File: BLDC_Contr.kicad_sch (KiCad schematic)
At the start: 100 parts, among them J1 XT60, J10 PH, J2 MR60, J3 Conn_ARM_SWD_TagConnect_TC2030, J4 PH, J5 PH, J6 PH, J7 PH, J8 PH, J9 PIN, Q1 CSD18540Q5B, Q2 CSD18540Q5B, Q3 CSD18540Q5B, Q4 CSD18540Q5B, Q5 CSD18540Q5B, Q6 CSD18540Q5B, U1 STM32G431CBU6, U2 DRV8323RSRGZR, U3 AMS1117-3.3, Y1 Crystal_16Mhz

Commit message: add PCB layouts
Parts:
- removed C2: 0.1u, Capacitor_SMD:C_0603_1608Metric, symbol Device:C_Small
- removed J2: MR60, Connector_AMASS:AMASS_MR30PW-M_1x03_P3.50mm_Horizontal, symbol Connector_Generic:Conn_01x03
- added H5, H6, H7: MountingHole_Pad_MP, MountingHole:MountingHole_2.5mm_Pad_Via, symbol Mechanical:MountingHole_Pad_MP
- C18: renamed from C19; footprint Capacitor_SMD:C_0603_1608Metric -> Capacitor_SMD:C_1210_3225Metric
- C19: renamed from C20; footprint Capacitor_SMD:C_0603_1608Metric -> Capacitor_SMD:C_1210_3225Metric
- D10, D13, D6, D8: footprint Package_TO_SOT_SMD:SOT-143 -> Diode_SMD:Nexperia_DSN1608-2_1.6x0.8mm; symbol Device:D_TVS -> Diode:PTVS5V0Z1USK
- D11: footprint Diode_SMD:D_0201_0603Metric -> Package_TO_SOT_SMD:SOT-23
- D12, D4, D5, D7, D9: footprint Package_TO_SOT_SMD:SOT-23-3 -> Package_TO_SOT_SMD:SOT-523
- J10: footprint Connector_JST:JST_PH_S4B-PH-K_1x04_P2.00mm_Horizontal -> Connector_JST:JST_PH_S5B-PH-K_1x05_P2.00mm_Horizontal
- J2: renamed from J3; footprint Connector:Tag-Connect_TC2030-IDC-FP_2x03_P1.27mm_Vertical -> Connector:Tag-Connect_TC2030-IDC-NL_2x03_P1.27mm_Vertical
- R10, R11, R12: value 3m -> 1m
- R21, R22: value 0 -> 56
- renumbered C11 to C10, C12 to C11, C13 to C12, C14 to C13, C15 to C14, C16 to C15, C17 to C16, C18 to C17, C3 to C2, C21 to C20, C22 to C21, C23 to C22, C24 to C23, C25 to C24, C26 to C25, C27 to C26, C28 to C27, C29 to C28, C30 to C29, C4 to C3, C36 to C30, C5 to C4, C6 to C5, C7 to C6, C8 to C7, C9 to C8, C10 to C9, J4 to J3, J5 to J4, J6 to J5, J7 to J6, J8 to J7, J9 to J8, Q2 to Q1, Q1 to Q2, Q4 to Q3, Q3 to Q4, Q6 to Q5, Q5 to Q6, R16 to R13, R13 to R14, R14 to R15, R15 to R16
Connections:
- net +3.3V: now also D10.1 (K), D6.1 (K), D8.1 (K); no longer C17.1, D10.2 (A2), D6.2 (A2), D8.2 (A2), U2.26 (VREF)
- net +3.3VA: now also C17.1, U2.26 (VREF)
- net +5V: now also D13.1 (K); no longer D13.2 (A2)
- net AMT_A_C: now also D12.1 (K); no longer D12.2 (K)
- net AMT_B_C: now also D12.2 (K); no longer D12.1 (K)
- net CAN_H_C: now also D11.2 (A2), J6.2 (Pin_2), J7.2 (Pin_2); no longer D11.1 (A1), J6.1 (Pin_1), J7.1 (Pin_1)
- net CAN_L_C: now also D11.1 (A1), J6.1 (Pin_1), J7.1 (Pin_1); no longer D11.2 (A2), J6.2 (Pin_2), J7.2 (Pin_2)
- net GND: now also D10.2 (A), D13.2 (A), D6.2 (A), D8.2 (A); no longer D10.1 (A1), D13.1 (A1), D6.1 (A1), D8.1 (A1)
- net SHA: now also H5.MP
- net SHB: now also H7.MP
- net SHC: now also H6.MP
- net SPI1_MISO_C: now also D5.2 (K); no longer D5.1 (K)
- net SPI1_MOSI_C: now also D4.1 (K); no longer D4.2 (K)
- net SPI1_NCS_C: now also D4.2 (K); no longer D4.1 (K)
- net SPI1_SCK_C: now also D5.1 (K); no longer D5.2 (K)
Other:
- moved on the sheet: C1, D10, D13, D6, D8

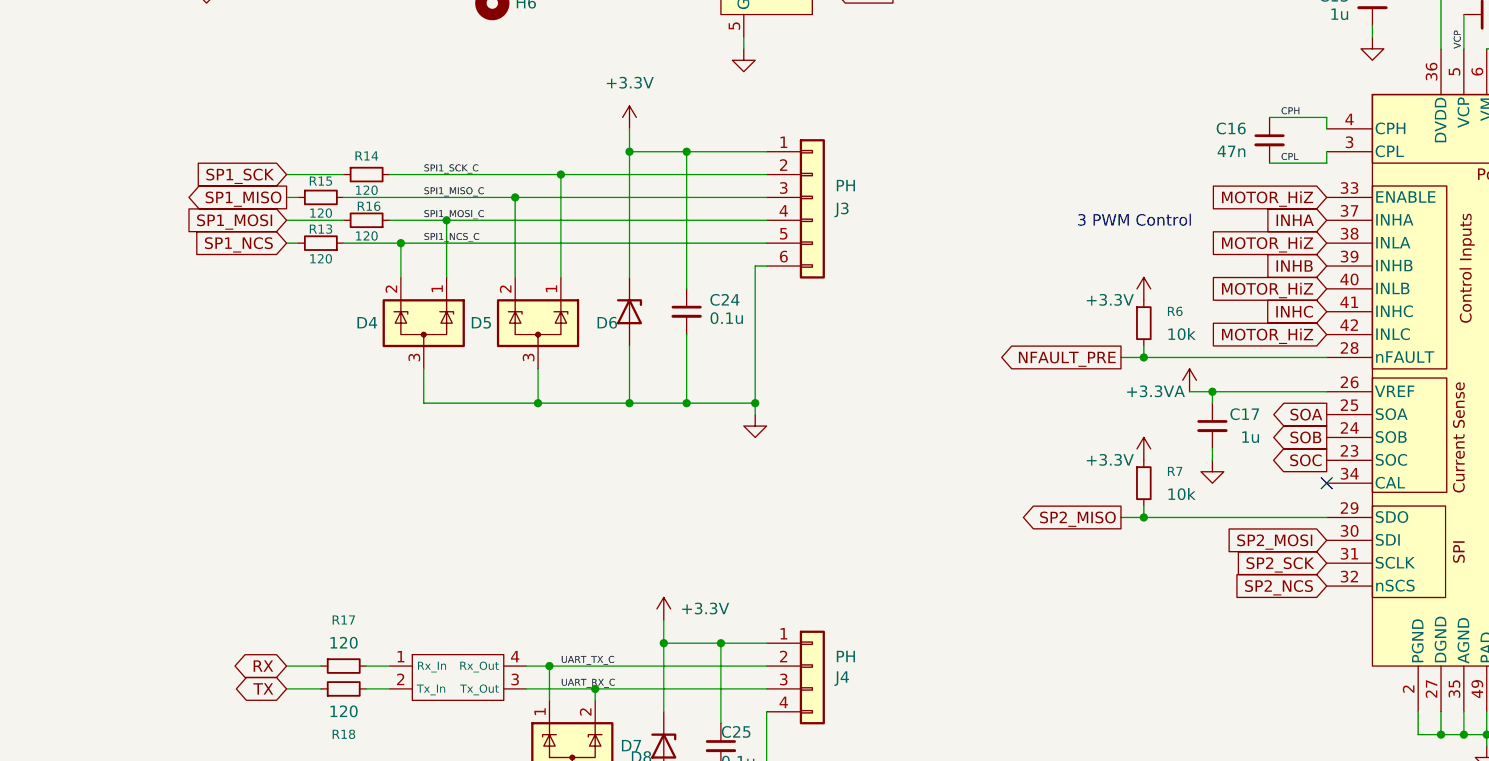
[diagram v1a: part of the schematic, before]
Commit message: add wiring. changed communication of spi on drv8323 from spi2 to spi1 for better wiring.
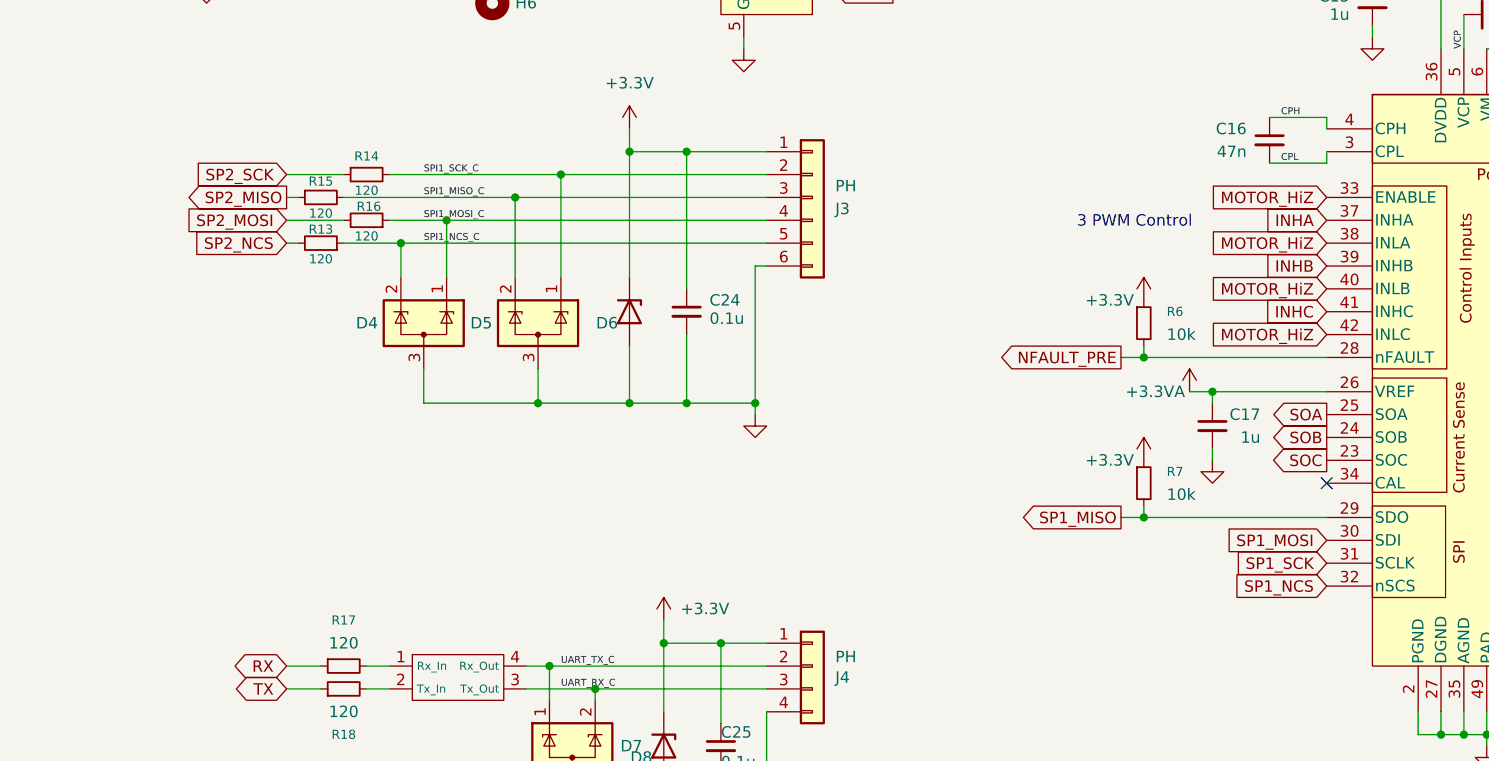
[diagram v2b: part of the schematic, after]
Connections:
- net SP1_MISO: now also R7.2, U2.29 (SDO); no longer R15.1
- net SP1_MOSI: now also U2.30 (SDI); no longer R16.2
- net SP1_NCS: now also U2.32 (nSCS); no longer R13.2
- net SP1_SCK: now also U2.31 (SCLK); no longer R14.1
- net SP2_MISO: now also R15.1; no longer R7.2, U2.29 (SDO)
- net SP2_MOSI: now also R16.2; no longer U2.30 (SDI)
- net SP2_NCS: now also R13.2; no longer U2.32 (nSCS)
- net SP2_SCK: now also R14.1; no longer U2.31 (SCLK)

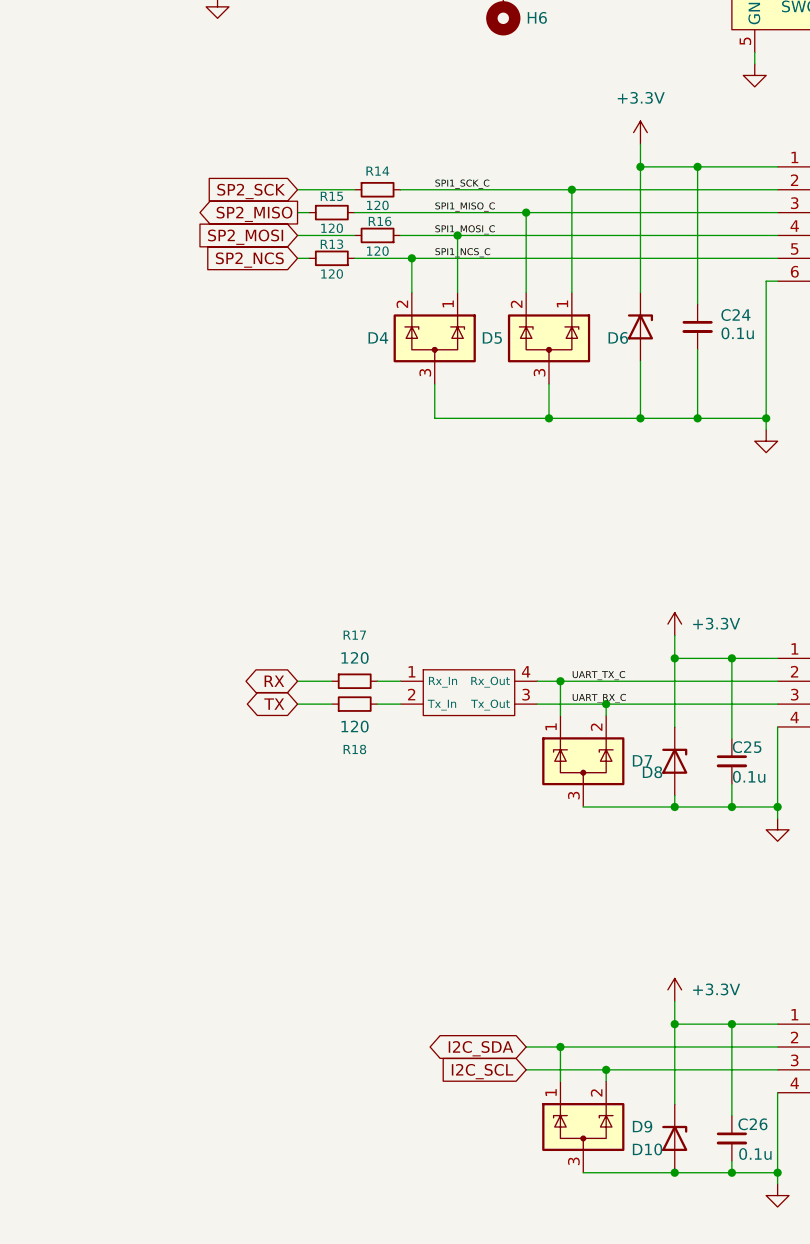
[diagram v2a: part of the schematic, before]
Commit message: added most wiring, not erc checked. changed pinouts on connectors for easier wiring
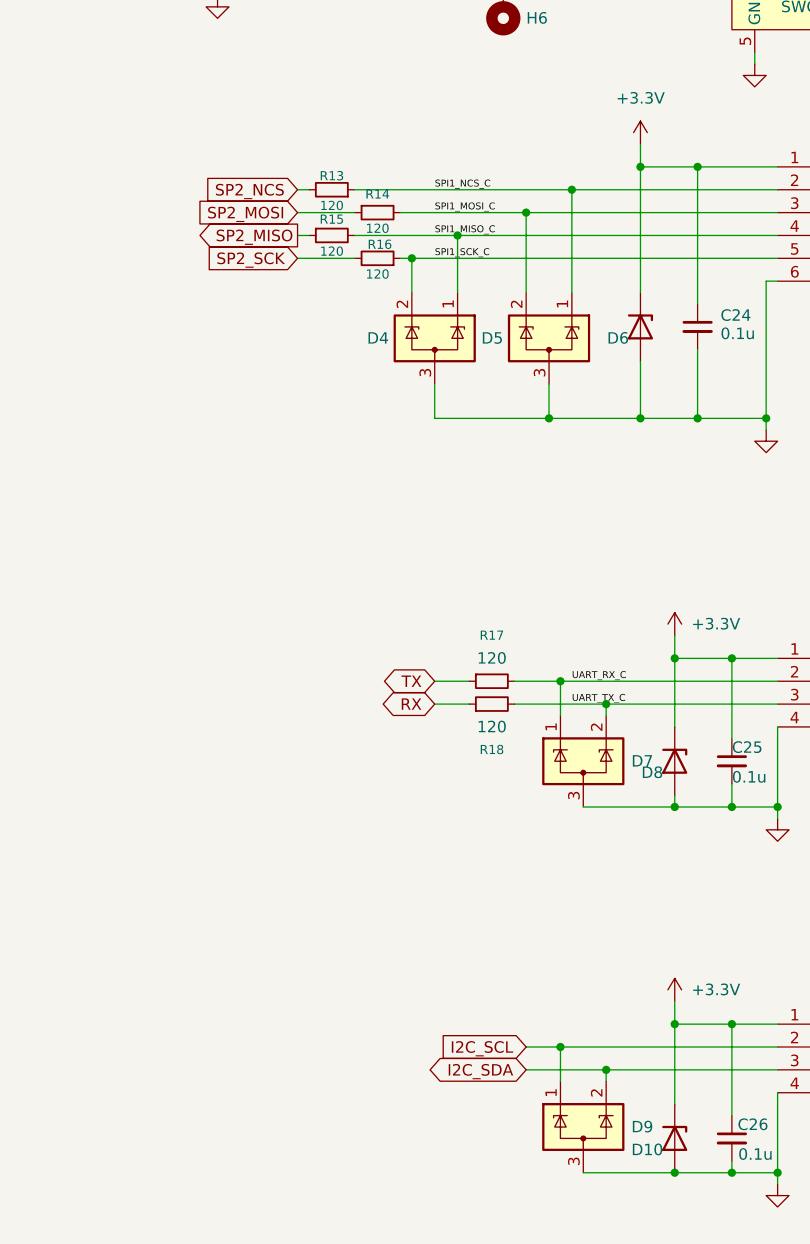
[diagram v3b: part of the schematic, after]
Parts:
- removed U5: ~, poka-yoke_rxtx:poka-yoke_rxtx, symbol poka-yoke_rxtx:poka_yoke_txrx
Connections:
- net I2C_SCL: now also D9.1 (K), J5.2 (Pin_2); no longer D9.2 (K), J5.3 (Pin_3)
- net I2C_SDA: now also D9.2 (K), J5.3 (Pin_3); no longer D9.1 (K), J5.2 (Pin_2)
- net RX: now also R18.1; no longer R17.1
- net SP2_MOSI: now also R14.1; no longer R16.2
- net SP2_SCK: now also R16.2; no longer R14.1
- net SPI1_MISO_C: now also D4.1 (K), J3.4 (Pin_4); no longer D5.2 (K), J3.3 (Pin_3)
- net SPI1_MOSI_C: now also D5.2 (K), J3.3 (Pin_3), R14.2; no longer D4.1 (K), J3.4 (Pin_4), R16.1
- net SPI1_NCS_C: now also D5.1 (K), J3.2 (Pin_2); no longer D4.2 (K), J3.5 (Pin_5)
- net SPI1_SCK_C: now also D4.2 (K), J3.5 (Pin_5), R16.1; no longer D5.1 (K), J3.2 (Pin_2), R14.2
- net TX: now also R17.1; no longer R18.1
- net UART_RX_C: now also D7.1 (K), J4.2 (Pin_2), R17.2; no longer D7.2 (K), J4.3 (Pin_3)
- net UART_TX_C: now also D7.2 (K), J4.3 (Pin_3), R18.2; no longer D7.1 (K), J4.2 (Pin_2)
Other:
- moved on the sheet: R13, R14, R15, R16, R17, R18

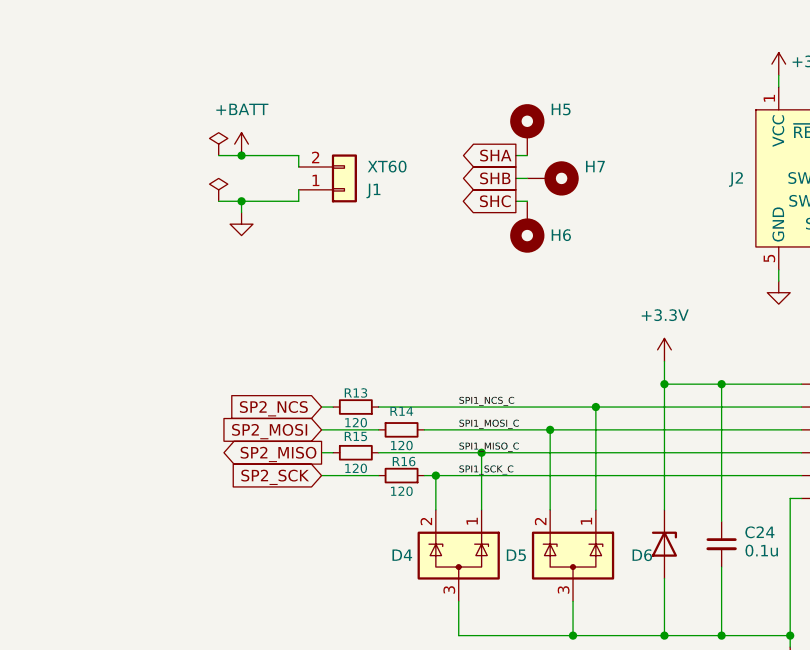
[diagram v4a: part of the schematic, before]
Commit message: changed most 0603 parts to 0402. wiring changed. pcb dimesion from 65*80mm to 60*80mm
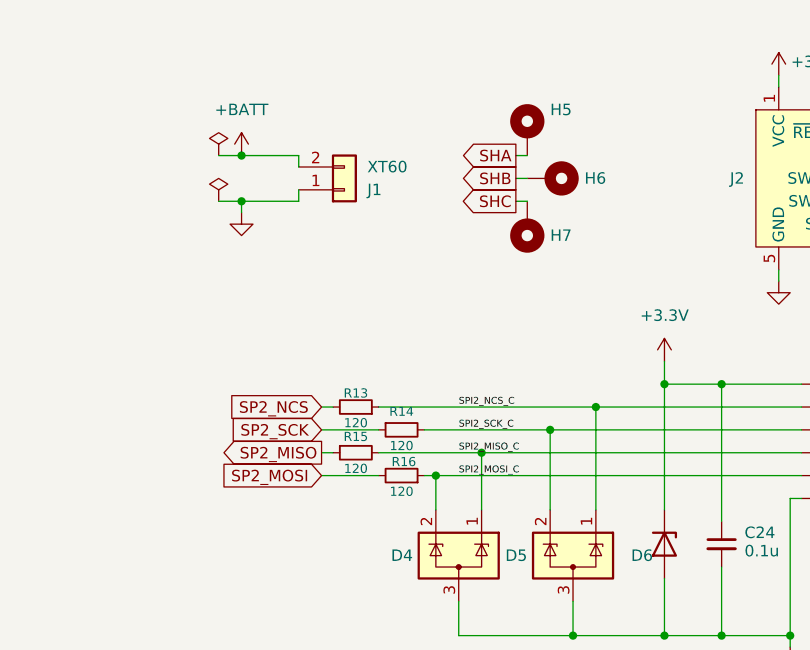
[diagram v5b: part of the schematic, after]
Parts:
- C1, C10, C11, C12, C13, C14, C15, C17, C2, C20, C23, C24, C25, C26, C27, C28, C29, C3, C4, C5, C7, C8, C9: footprint Capacitor_SMD:C_0603_1608Metric -> Capacitor_SMD:C_0402_1005Metric
- H1, H2, H3, H4: footprint MountingHole:MountingHole_3.2mm_M3_DIN965_Pad_TopBottom -> MountingHole:MountingHole_3.2mm_M3_Pad_Via
- R1, R13, R14, R15, R16, R17, R18, R19, R2, R20, R21, R22, R3, R4, R5, R6, R7, R8: footprint Resistor_SMD:R_0603_1608Metric -> Resistor_SMD:R_0402_1005Metric
- R9: footprint Resistor_SMD:R_0603_1608Metric -> Resistor_SMD:R_0805_2012Metric
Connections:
- net SHB: now also H6.MP; no longer H7.MP
- net SHC: now also H7.MP; no longer H6.MP
- net SP2_MOSI: now also R16.2; no longer R14.1
- net SP2_SCK: now also R14.1; no longer R16.2
- net SPI1_MISO_C renamed SPI2_MISO_C
- net SPI1_MOSI_C renamed SPI2_SCK_C
- net SPI1_NCS_C renamed SPI2_NCS_C
- net SPI1_SCK_C renamed SPI2_MOSI_C
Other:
- moved on the sheet: H6, H7

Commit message: DRCing not done
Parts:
- H1, H2, H3, H4: footprint MountingHole:MountingHole_3.2mm_M3_Pad_Via -> MountingHole:MountingHole_3.2mm_M3_Pad_TopBottom
- H5, H6, H7: footprint MountingHole:MountingHole_2.5mm_Pad_Via -> MountingHole:MountingHole_2.5mm_Pad_TopBottom
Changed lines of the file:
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@@
 			)
 		)
-		(property "Footprint" "MountingHole:MountingHole_2.5mm_Pad_Via"
+		(property "Footprint" "MountingHole:MountingHole_2.5mm_Pad_TopBottom"
 			(at 194.31 39.37 0)
 			(effects
@@
 			)
 		)
-		(property "Footprint" "MountingHole:MountingHole_3.2mm_M3_Pad_Via"
+		(property "Footprint" "MountingHole:MountingHole_3.2mm_M3_Pad_TopBottom"
 			(at 76.2 232.41 0)
 			(effects
@@
 			)
 		)
-		(property "Footprint" "MountingHole:MountingHole_2.5mm_Pad_Via"
+		(property "Footprint" "MountingHole:MountingHole_2.5mm_Pad_TopBottom"
 			(at 196.85 34.29 0)
 			(effects
@@
 			)
 		)
-		(property "Footprint" "MountingHole:MountingHole_2.5mm_Pad_Via"
+		(property "Footprint" "MountingHole:MountingHole_2.5mm_Pad_TopBottom"
 			(at 194.31 29.21 0)
 			(effects
@@
 			)
 		)
-		(property "Footprint" "MountingHole:MountingHole_3.2mm_M3_Pad_Via"
+		(property "Footprint" "MountingHole:MountingHole_3.2mm_M3_Pad_TopBottom"
 			(at 63.5 232.41 0)
 			(effects
@@
 			)
 		)
-		(property "Footprint" "MountingHole:MountingHole_3.2mm_M3_Pad_Via"
+		(property "Footprint" "MountingHole:MountingHole_3.2mm_M3_Pad_TopBottom"
 			(at 101.6 232.41 0)
 			(effects
@@
 			)
 		)
-		(property "Footprint" "MountingHole:MountingHole_3.2mm_M3_Pad_Via"
+		(property "Footprint" "MountingHole:MountingHole_3.2mm_M3_Pad_TopBottom"
 			(at 88.9 232.41 0)
 			(effects

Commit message: changed most 0603 parts to 0402. wiring changed. pcb dimesion from 65*80mm to 60*80m
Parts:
- H1, H2, H3, H4: footprint MountingHole:MountingHole_3.2mm_M3_Pad_TopBottom -> MountingHole:MountingHole_3.2mm_M3
- H5, H6, H7: footprint MountingHole:MountingHole_2.5mm_Pad_TopBottom -> MountingHole:MountingHole_2.5mm
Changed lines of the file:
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@@
 			)
 		)
-		(property "Footprint" "MountingHole:MountingHole_2.5mm_Pad_TopBottom"
+		(property "Footprint" "MountingHole:MountingHole_2.5mm"
 			(at 194.31 39.37 0)
 			(effects
@@
 			)
 		)
-		(property "Footprint" "MountingHole:MountingHole_3.2mm_M3_Pad_TopBottom"
+		(property "Footprint" "MountingHole:MountingHole_3.2mm_M3"
 			(at 76.2 232.41 0)
 			(effects
@@
 			)
 		)
-		(property "Footprint" "MountingHole:MountingHole_2.5mm_Pad_TopBottom"
+		(property "Footprint" "MountingHole:MountingHole_2.5mm"
 			(at 196.85 34.29 0)
 			(effects
@@
 			)
 		)
-		(property "Footprint" "MountingHole:MountingHole_2.5mm_Pad_TopBottom"
+		(property "Footprint" "MountingHole:MountingHole_2.5mm"
 			(at 194.31 29.21 0)
 			(effects
@@
 			)
 		)
-		(property "Footprint" "MountingHole:MountingHole_3.2mm_M3_Pad_TopBottom"
+		(property "Footprint" "MountingHole:MountingHole_3.2mm_M3"
 			(at 63.5 232.41 0)
 			(effects
@@
 			)
 		)
-		(property "Footprint" "MountingHole:MountingHole_3.2mm_M3_Pad_TopBottom"
+		(property "Footprint" "MountingHole:MountingHole_3.2mm_M3"
 			(at 101.6 232.41 0)
 			(effects
@@
 			)
 		)
-		(property "Footprint" "MountingHole:MountingHole_3.2mm_M3_Pad_TopBottom"
+		(property "Footprint" "MountingHole:MountingHole_3.2mm_M3"
 			(at 88.9 232.41 0)
 			(effects
